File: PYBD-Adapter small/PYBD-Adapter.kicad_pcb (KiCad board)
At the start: 2 copper layers, 18.3 x 41.9 mm, 5 parts, among them J1 Conn_01x16, J2 Conn_01x16, J3 Conn_01x16, J4 Conn_01x16

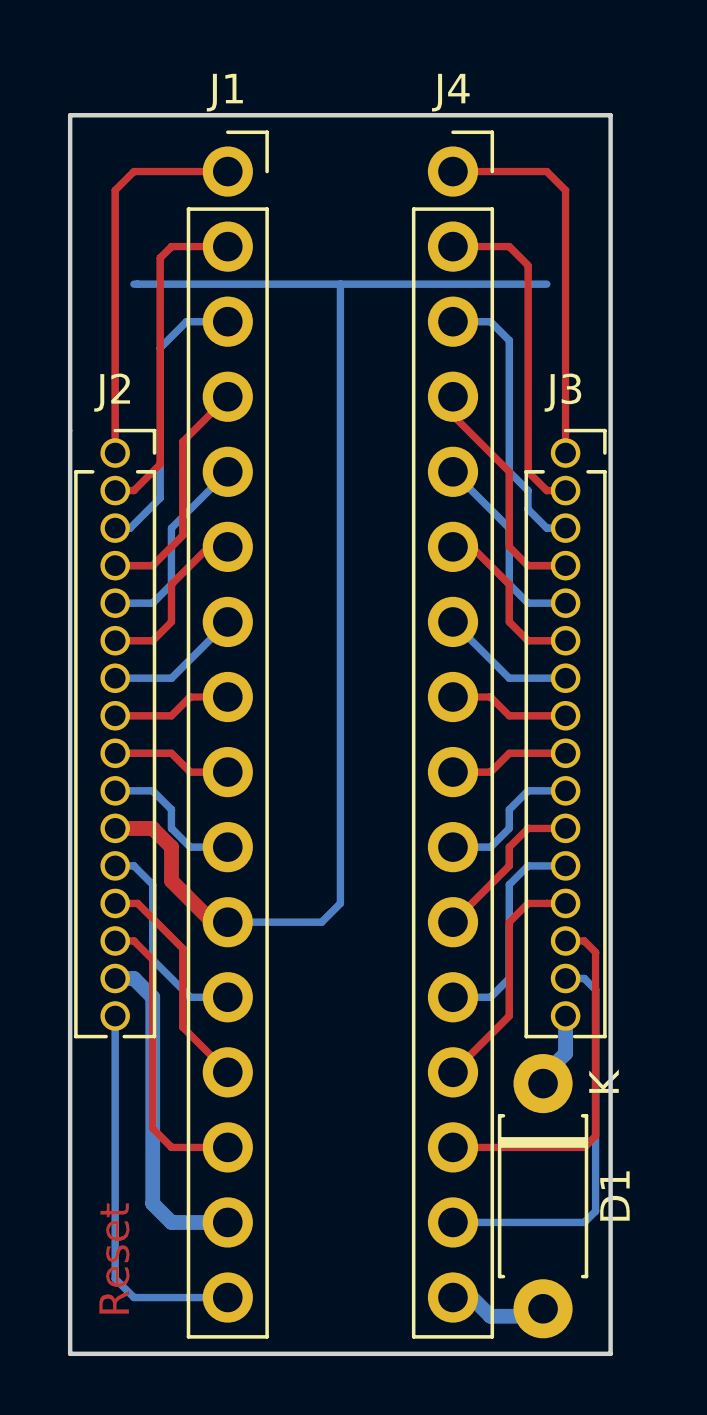
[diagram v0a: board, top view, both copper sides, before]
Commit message: Small Adapter: Add switches for reset and boot
Change diode pad to hold SMD parts.
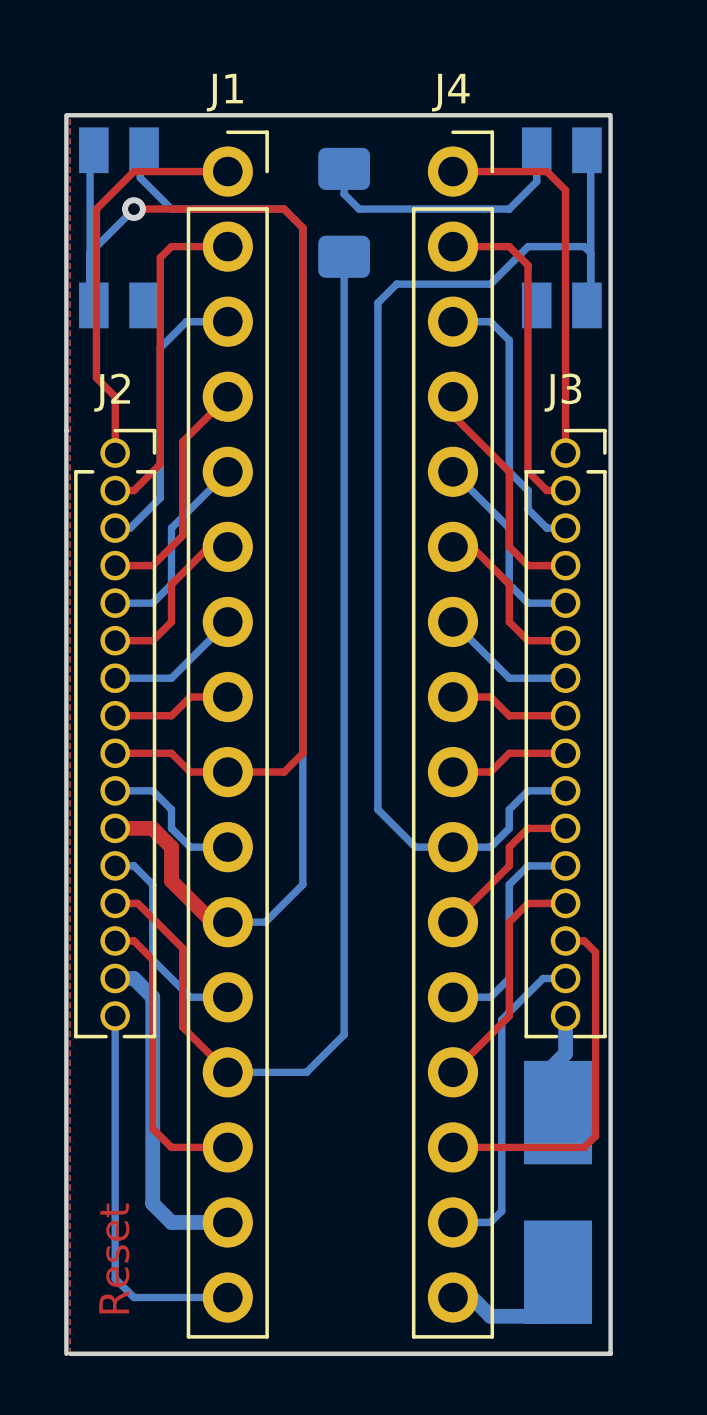
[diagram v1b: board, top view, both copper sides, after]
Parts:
- added R1: 10k, Resistor_SMD:R_1206_3216Metric_Pad1.42x1.75mm_HandSolder, B.Cu at (139.8, 90.9)
- added SW1: Reset, Button_Switch_SMD:Panasonic_EVQPUJ_EVQPUA, B.Cu at (132.2, 91.4)
- added SW2: Boot, Button_Switch_SMD:Panasonic_EVQPUJ_EVQPUA, B.Cu at (147.2, 91.4)
- D1: value D_Schottky -> 1N5817; footprint Diode_THT:D_DO-41_SOD81_P7.62mm_Horizontal -> Diode_SMD:D_SMB_Handsoldering; moved to B.Cu
- J1, J4: value Conn_01x16 -> Socket Strip 0.1"
- J2, J3: value Conn_01x16 -> Socket Strip 0.05"
- moved D1 3.72 mm to (147.1, 124.1)
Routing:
- net Net-(J1-Pad9): track 4.07 -> 39.8 mm, vias 0 -> 1
- net Net-(J3-Pad10): track 4.97 -> 40.3 mm
- net Net-(J1-Pad13): track 7.74 -> 38.5 mm
- net Net-(R1-Pad1): track 0.00 -> 9.03 mm
- net GND: track 44.8 -> 38.2 mm
- net Net-(J3-Pad15): track 13.7 -> 11.0 mm
- net Net-(J1-Pad1): track 13.0 -> 13.5 mm
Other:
- board size 18.3 x 41.9 mm -> 18.4 x 41.9 mm
- board text added: "Boot"
- board text added: "USB"

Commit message: Small Adapter: Add mounting holes for the switch
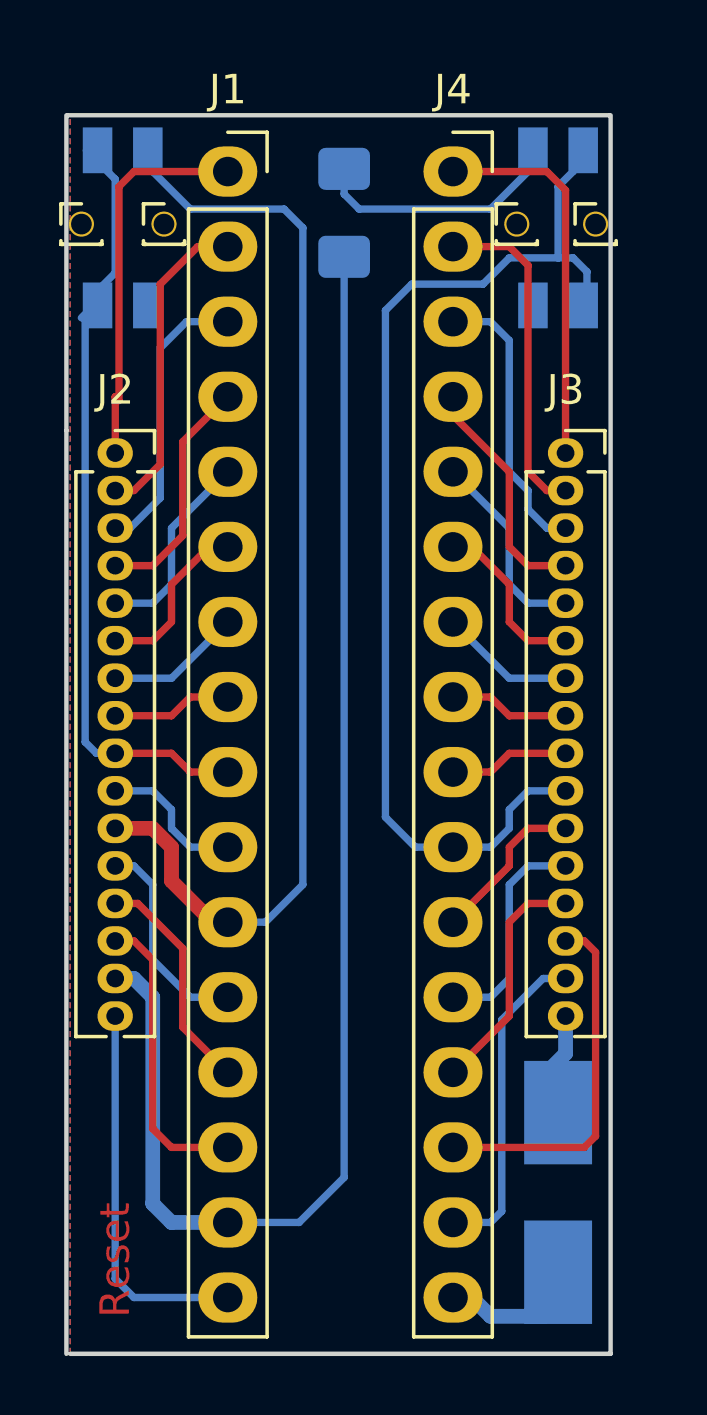
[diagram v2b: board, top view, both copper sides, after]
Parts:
- added REF**: PinHeader_1x01_P1.00mm_Vertical, Connector_PinHeader_1.00mm:PinHeader_1x01_P1.00mm_Vertical, F.Cu at (130.9, 91.3)
- added REF**: PinHeader_1x01_P1.00mm_Vertical, Connector_PinHeader_1.00mm:PinHeader_1x01_P1.00mm_Vertical, F.Cu at (133.7, 91.3)
- added REF**: PinHeader_1x01_P1.00mm_Vertical, Connector_PinHeader_1.00mm:PinHeader_1x01_P1.00mm_Vertical, F.Cu at (145.7, 91.3)
- added REF**: PinHeader_1x01_P1.00mm_Vertical, Connector_PinHeader_1.00mm:PinHeader_1x01_P1.00mm_Vertical, F.Cu at (148.3, 91.3)
- R1: value 10k -> 51k
- moved SW1 0.13 mm to (132.3, 91.4)
- moved SW2 0.13 mm to (147.1, 91.4)
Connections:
- R1 pad 2: Net-(J1-Pad13) -> Net-(J1-Pad15)
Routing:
- net Net-(J1-Pad15): track 11.3 -> 47.1 mm
- net Net-(J1-Pad13): track 38.5 -> 7.74 mm
- net Net-(J1-Pad9): track 39.8 -> 26.1 mm, vias 1 -> 0
- net Net-(J3-Pad10): track 40.3 -> 37.7 mm
- net Net-(J1-Pad2): track 11.3 -> 10.8 mm
